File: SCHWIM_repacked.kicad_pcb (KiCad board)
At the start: 2 copper layers, 17.9 x 35.8 mm, 7 parts, among them J1 SWIM Connector, U1 74HCT244, U2 74HCT32

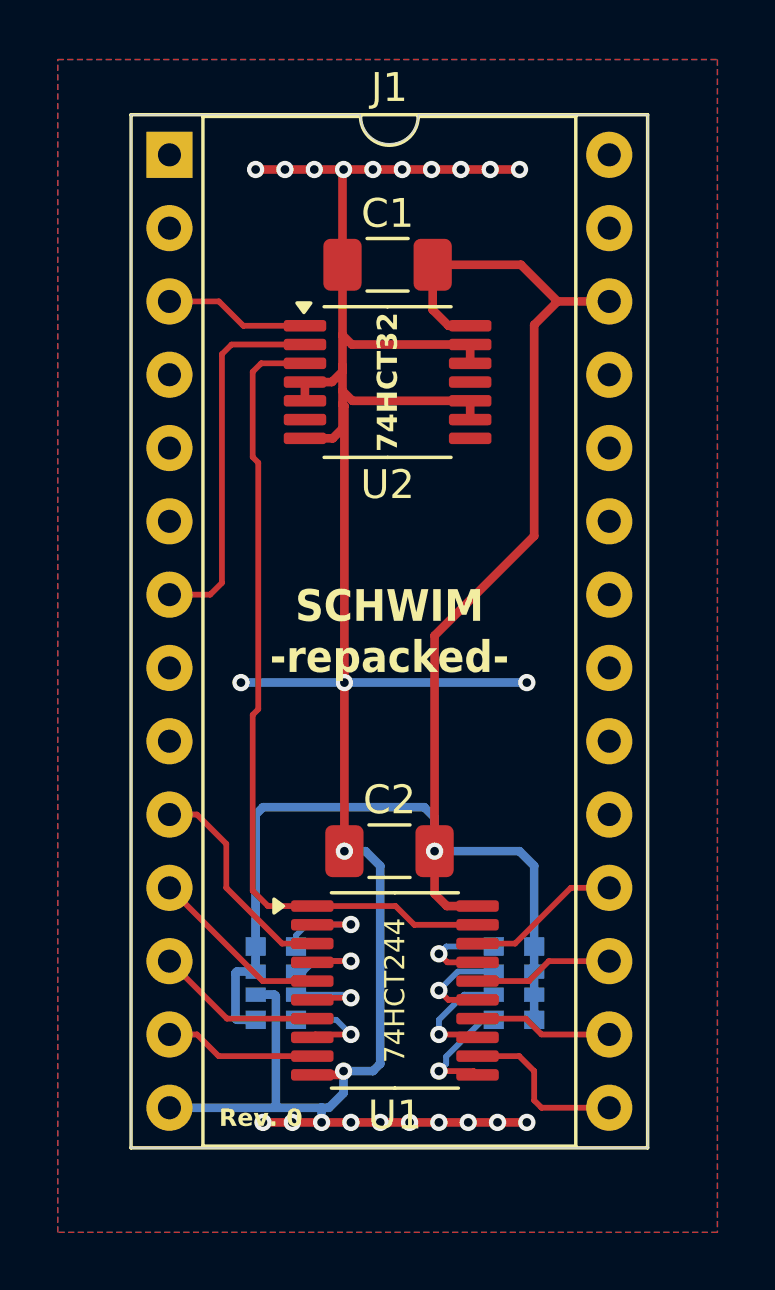
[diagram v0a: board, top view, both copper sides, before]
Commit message: Use a single or gate
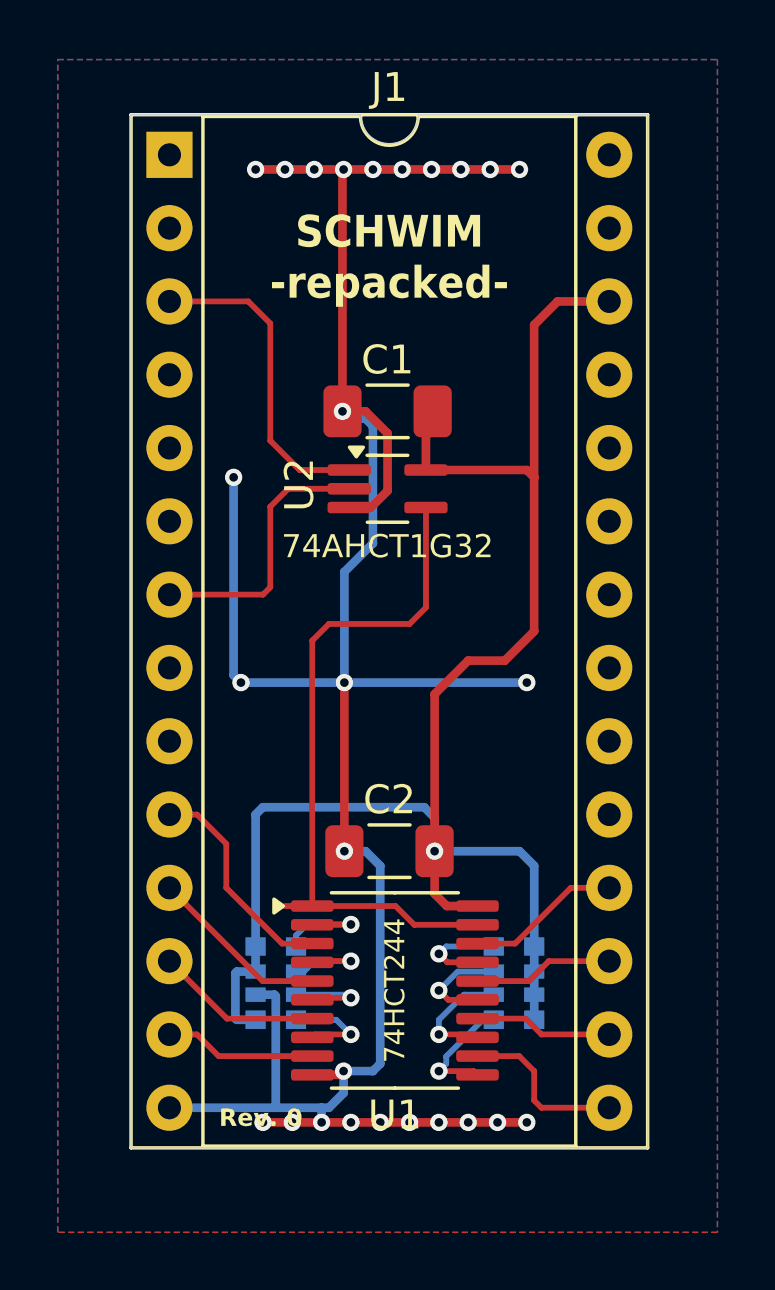
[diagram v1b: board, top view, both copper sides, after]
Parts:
- U2: value 74HCT32 -> 74AHCT1G32; footprint Package_SO:TSSOP-14_4.4x5mm_P0.65mm -> Package_TO_SOT_SMD:SOT-353_SC-70-5_Handsoldering
- moved C1 5.08 mm to (95.2, 68.1)
- moved U2 3.70 mm to (95.2, 70.8)
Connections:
- U2 pad 3: /CONTROL -> GND
- U2 pad 4: GND -> /CONTROL
- U2 pad 5: GND -> VCC
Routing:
- net /A0: track 5.05 -> 11.0 mm
- net /CONTROL: track 28.4 -> 24.0 mm
- net /~{DEV}: track 12.9 -> 9.38 mm
- net VCC: track 58.8 -> 57.5 mm
- net GND: track 89.9 -> 88.6 mm, vias 25 -> 27

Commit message: Added rev.1 of the repacked schwim, fixed footprint for U2
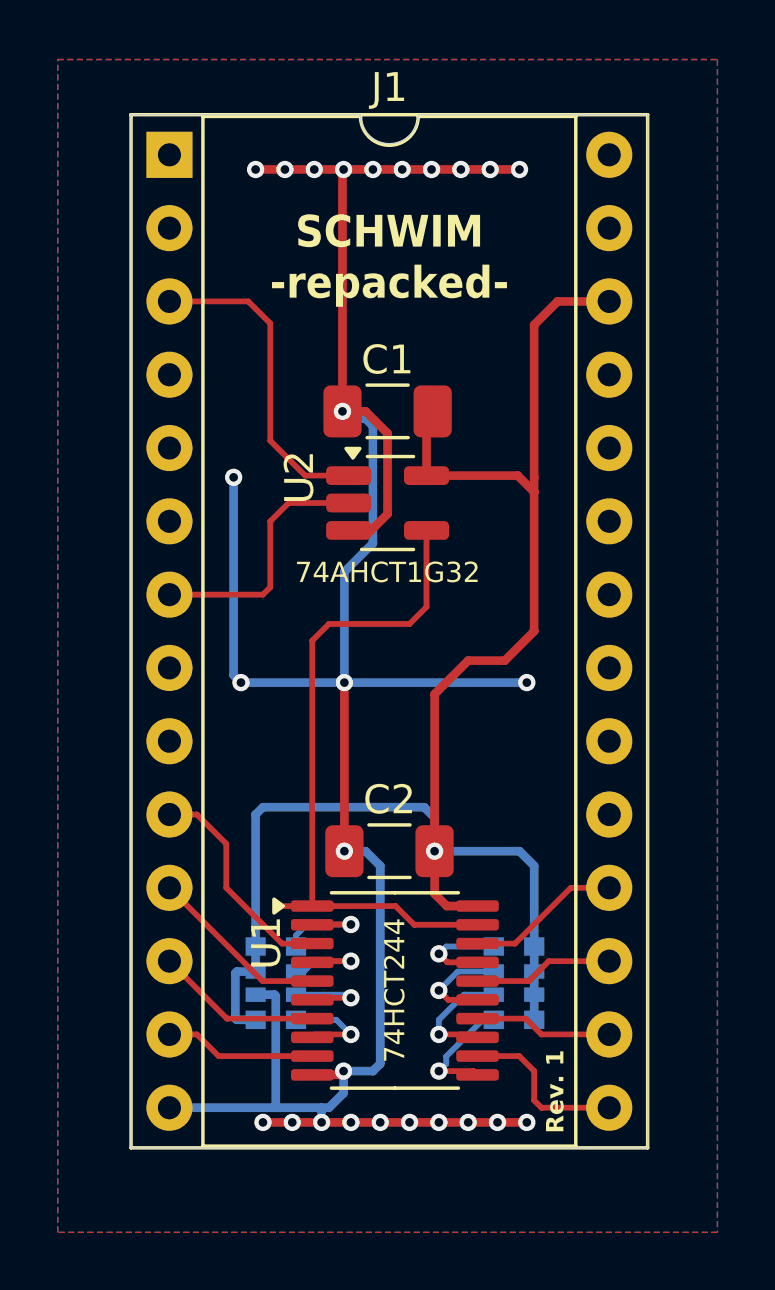
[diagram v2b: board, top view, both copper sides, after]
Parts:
- U2: footprint Package_TO_SOT_SMD:SOT-353_SC-70-5_Handsoldering -> Package_TO_SOT_SMD:SOT-23-5_HandSoldering
- moved U2 0.49 mm to (95.2, 71.2)
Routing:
- net GND: track 88.6 -> 89.5 mm
- net /CONTROL: track 24.0 -> 23.2 mm
- net VCC: track 57.5 -> 58.2 mm
- net /~{DEV}: track 9.38 -> 8.86 mm
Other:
- board text added: "Rev. 1"
- board text removed: "Rev. 0"
